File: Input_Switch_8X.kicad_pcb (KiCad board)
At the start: 2 copper layers, 133 x 50 mm, 86 parts, among them J1 Conn_01x02, J10 GND, J2 Conn_01x02, J3 Conn_01x02, J4 Conn_01x02, J5 Conn_01x02, J6 Conn_01x02, J7 Conn_01x02, J8 Conn_01x02, J9 VCC, Q1 AO3400A, Q10 AO3400A, Q11 BC817, Q12 AO3400A, Q13 BC817, Q14 AO3400A, Q15 BC817, Q16 AO3400A, Q2 BC817, Q3 BC817, Q4 AO3400A, Q5 BC817, Q6 AO3400A, Q7 BC817, Q8 AO3400A, Q9 BC817, SW1 SW_Push, SW10 SW_SPST, SW11 SW_Push, SW12 SW_SPST, SW13 SW_Push, SW14 SW_SPST, SW15 SW_Push, SW16 SW_SPST, SW2 SW_SPST, SW3 SW_Push, SW4 SW_SPST, SW5 SW_Push, SW6 SW_SPST, SW7 SW_Push, SW8 SW_SPST, SW9 SW_Push

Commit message: update footprint
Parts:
- D1, D10, D12, D14, D16, D4, D6, D8: footprint LED_SMD:LED_0603_1608Metric -> Library:LED_0603_1608Metric
- H1, H2, H3, H4: footprint MountingHole:MountingHole_3.2mm_M3_Pad_Via -> Library:MountingHole_3.2mm_M3_Pad_Via
- J1, J2, J3, J4, J5, J6, J7, J8: footprint Connector_PinHeader_2.54mm:PinHeader_1x02_P2.54mm_Vertical -> Library:PinHeader_1x02_P2.54mm_Vertical
- J10, J9: footprint Connector_PinHeader_2.54mm:PinHeader_2x02_P2.54mm_Vertical -> Library:PinHeader_2x02_P2.54mm_Vertical
- Q1, Q10, Q11, Q12, Q13, Q14, Q15, Q16, Q2, Q3, Q4, Q5, Q6, Q7, Q8, Q9: footprint Package_TO_SOT_SMD:SOT-23 -> Library:SOT-23
- R1, R10, R11, R12, R13, R14, R15, R16, R17, R18, R19, R2, R20, R21, R22, R23, R24, R3, R4, R5, R6, R7, R8, R9: footprint Resistor_SMD:R_0603_1608Metric -> Library:R_0603_1608Metric
- moved J9 16.4 mm to (78.3, 77.0), turned to 180 degrees
- moved J10 11.5 mm to (78.3, 63.3), turned to 180 degrees
- turned R10 to -90 degrees
- turned R11 to -90 degrees
- turned R12 to -90 degrees
- turned R13 to -90 degrees
- turned R14 to -90 degrees
- turned R16 to -90 degrees
- turned R17 to -90 degrees
- turned R19 to -90 degrees
- turned R20 to -90 degrees
- turned R22 to -90 degrees
- turned R23 to -90 degrees
- turned R8 to -90 degrees
- turned R9 to -90 degrees
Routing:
- net VCC: track 0.00 -> 372.5 mm
- net /Switch_LED_2/Output: track 0.00 -> 54.3 mm, vias 0 -> 1
- net /Switch_LED_5/Output: track 0.00 -> 54.1 mm, vias 0 -> 1
- net /Switch_LED_4/Output: track 0.00 -> 54.1 mm, vias 0 -> 1
- net /Switch_LED_7/Output: track 0.00 -> 54.1 mm, vias 0 -> 1
- net /Switch_LED_6/Output: track 0.00 -> 54.1 mm, vias 0 -> 1
- net /Switch_LED_1/Output: track 0.00 -> 54.1 mm, vias 0 -> 1
- net /Switch_LED_8/Output: track 0.00 -> 54.1 mm, vias 0 -> 1
- net /Switch_LED_3/Output: track 0.00 -> 54.1 mm, vias 0 -> 1
- net Net-(D13-K): track 0.00 -> 12.1 mm
- net Net-(D11-K): track 0.00 -> 12.0 mm
- net Net-(D5-K): track 0.00 -> 12.0 mm
- net Net-(D9-K): track 0.00 -> 11.9 mm
- net Net-(D7-K): track 0.00 -> 11.9 mm
- net Net-(D15-K): track 0.00 -> 11.9 mm
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- added copper zone on B.Cu, net GND
- added copper zone on F.Cu, net GND

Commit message: update
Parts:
- H1, H2, H3, H4: footprint Library:MountingHole_3.2mm_M3_Pad_Via -> MountingHole:MountingHole_3.2mm_M3_Pad_Via
- J10, J9: footprint Library:PinHeader_2x02_P2.54mm_Vertical -> Connector_PinHeader_2.54mm:PinHeader_2x02_P2.54mm_Vertical
- R1, R15, R18, R2, R21, R24, R3, R4: value 33 -> 33R

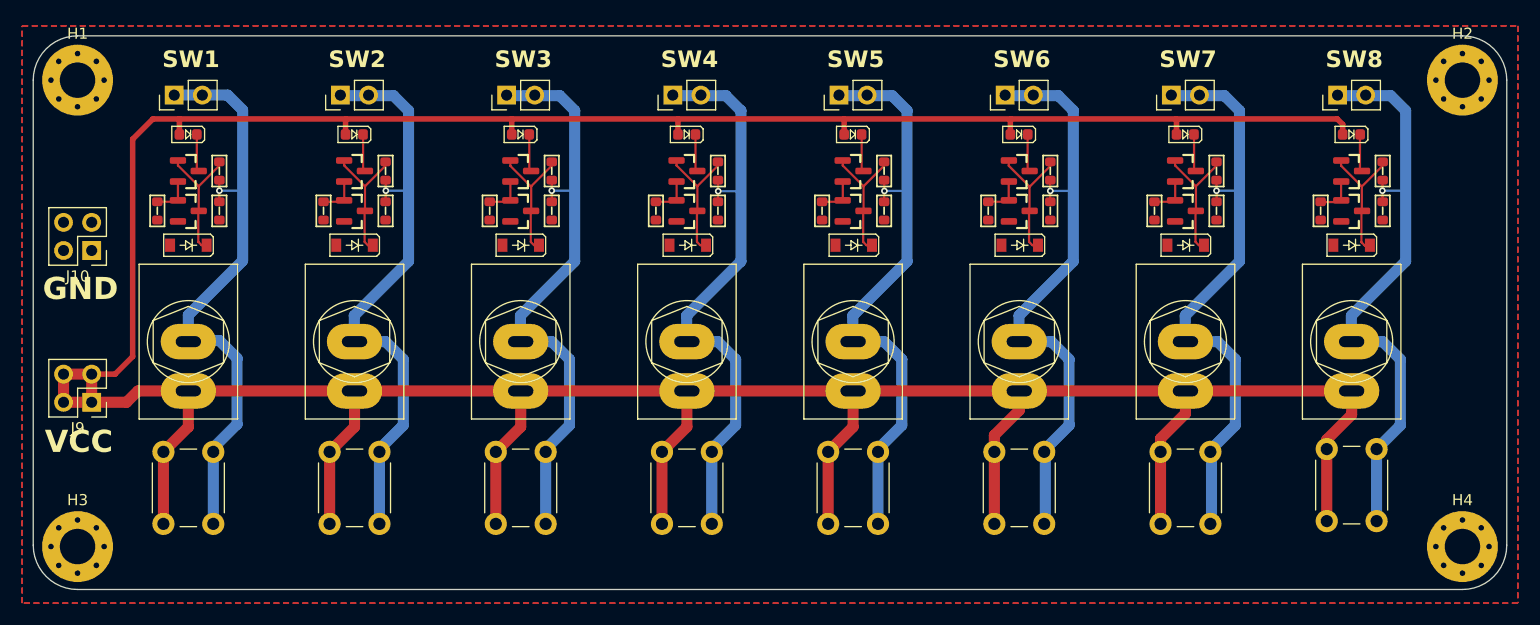
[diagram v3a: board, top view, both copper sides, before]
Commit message: Remove the now ignored directory
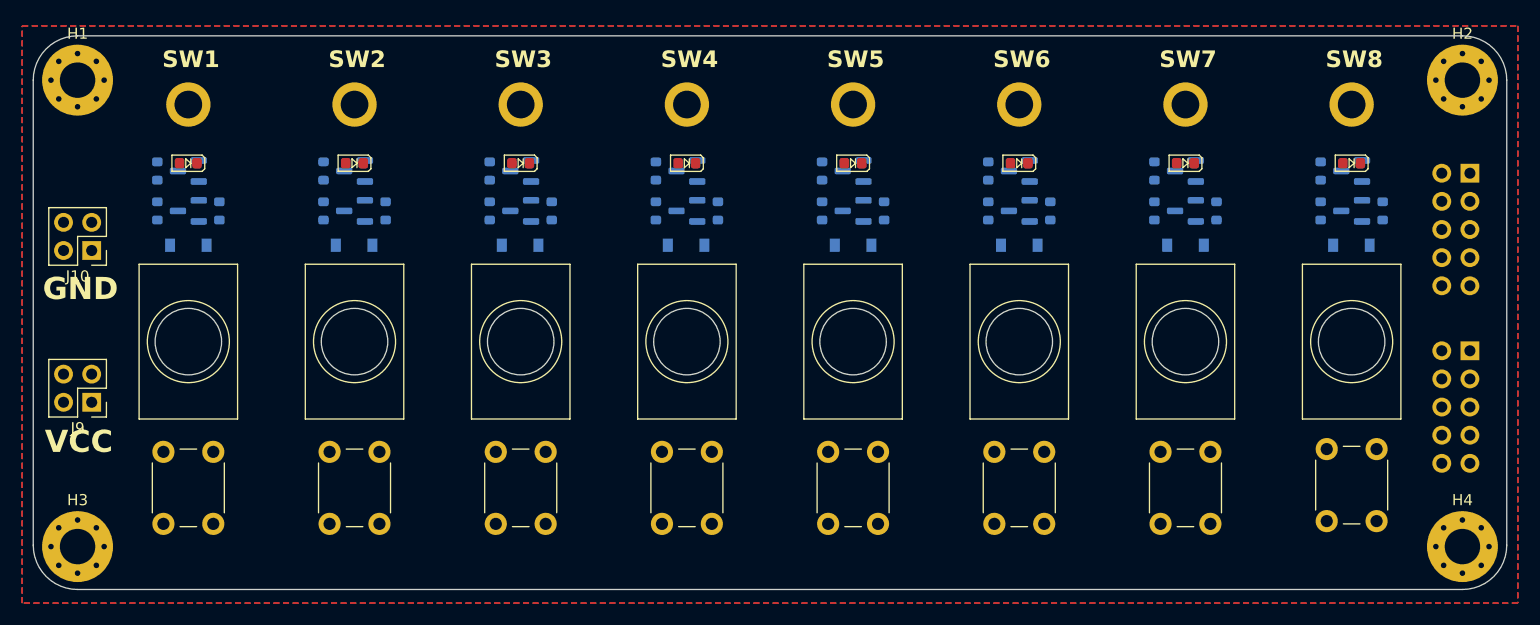
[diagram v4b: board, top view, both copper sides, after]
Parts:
- added REF**: PinHeader_2x05_P2.54mm_Vertical, Library:PinHeader_2x05_P2.54mm_Vertical, B.Cu at (202.7, 72.3)
- added REF**: PinHeader_2x05_P2.54mm_Vertical, Library:PinHeader_2x05_P2.54mm_Vertical, B.Cu at (202.7, 56.3)
- D11, D13, D15, D2, D3, D5, D7, D9, Q1, Q10, Q11, Q12, Q13, Q14, Q15, Q16, Q2, Q3, Q4, Q5, Q6, Q7, Q8, Q9, R1, R10, R11, R12, R13, R14, R15, R16, R17, R18, R19, R2, R20, R21, R22, R23, R24, R3, R4, R5, R6, R7, R8, R9: moved to B.Cu
- H1, H2, H3, H4: footprint MountingHole:MountingHole_3.2mm_M3_Pad_Via -> Library:MountingHole_3.2mm_M3_Pad_Via
- J1, J2, J3, J4, J5, J6, J7, J8: footprint Library:PinHeader_1x02_P2.54mm_Vertical -> Library:MountingHole_2.5mm_Pad
- J10, J9: footprint Connector_PinHeader_2.54mm:PinHeader_2x02_P2.54mm_Vertical -> Library:PinHeader_2x02_P2.54mm_Vertical
- SW10, SW12, SW14, SW16, SW2, SW4, SW6, SW8: footprint Library:SW_Toggle_Blue_wSlots_2_Pins -> Library:SW_Toggle_Blue_wSlots_Nut
- moved R16 65.6 mm to (99.2, 59.7)
- moved R17 65.6 mm to (99.2, 56.1)
- moved R2 65.6 mm to (164.8, 59.7)
- moved D11 60.1 mm to (102.0, 62.8), turned to 0 degrees
- moved D3 60.0 mm to (162.0, 62.8), turned to 0 degrees
- moved Q11 60.0 mm to (102.0, 59.7), turned to 180 degrees
- moved Q12 60.0 mm to (102.0, 56.1), turned to 180 degrees
- moved Q3 60.0 mm to (162.0, 59.7), turned to 180 degrees
- moved Q4 60.0 mm to (162.0, 56.1), turned to 180 degrees
- moved R18 54.4 mm to (104.8, 59.7)
- moved R7 54.4 mm to (159.2, 59.7)
- moved R8 54.4 mm to (159.2, 56.1)
- moved R13 35.6 mm to (114.2, 59.7)
- moved R14 35.6 mm to (114.2, 56.1)
- moved R3 35.6 mm to (149.8, 59.7)
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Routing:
- net VCC: track 372.5 -> 0.00 mm
- net /Switch_LED_2/Output: track 54.3 -> 0.00 mm, vias 1 -> 0
- net /Switch_LED_5/Output: track 54.1 -> 0.00 mm, vias 1 -> 0
- net /Switch_LED_4/Output: track 54.1 -> 0.00 mm, vias 1 -> 0
- net /Switch_LED_7/Output: track 54.1 -> 0.00 mm, vias 1 -> 0
- net /Switch_LED_6/Output: track 54.1 -> 0.00 mm, vias 1 -> 0
- net /Switch_LED_1/Output: track 54.1 -> 0.00 mm, vias 1 -> 0
- net /Switch_LED_8/Output: track 54.1 -> 0.00 mm, vias 1 -> 0
- net /Switch_LED_3/Output: track 54.1 -> 0.00 mm, vias 1 -> 0
- net Net-(D13-K): track 12.1 -> 0.00 mm
- net Net-(D11-K): track 12.0 -> 0.00 mm
- net Net-(D5-K): track 12.0 -> 0.00 mm
- net Net-(D9-K): track 11.9 -> 0.00 mm
- net Net-(D7-K): track 11.9 -> 0.00 mm
- net Net-(D15-K): track 11.9 -> 0.00 mm
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
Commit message: update
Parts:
- added REF**: MountingHole_2.1mm, MountingHole:MountingHole_2.1mm, F.Cu at (77.0, 47.9)
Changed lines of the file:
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@@
 			)
 		)
+		(model "${KIPRJMOD}/3D/24.106.STEP"
+			(offset
+				(xyz 0 0 3.81)
+			)
+			(scale
+				(xyz 1 1 1)
+			)
+			(rotate
+				(xyz 0 0 0)
+			)
+		)
 	)
 	(footprint "Library:MountingHole_2.5mm_Pad"
@@
 			)
 		)
+		(model "${KIPRJMOD}/3D/24.106.STEP"
+			(offset
+				(xyz 0 0 3.81)
+			)
+			(scale
+				(xyz 1 1 1)
+			)
+			(rotate
+				(xyz 0 0 0)
+			)
+		)
 	)
 	(footprint "Library:LED_0603_1608Metric"
@@
 			)
 		)
+		(model "${KIPRJMOD}/3D/24.106.STEP"
+			(offset
+				(xyz 0 0 3.81)
+			)
+			(scale
+				(xyz 1 1 1)
+			)
+			(rotate
+				(xyz 0 0 0)
+			)
+		)
 	)
 	(footprint "Library:SW_Toggle_Blue_wSlots_Nut"
@@
 		)
 	)
+	(footprint "MountingHole:MountingHole_2.1mm"
+		(layer "F.Cu")
+		(at 77 47.9)
+		(descr "Mounting Hole 2.1mm, no annular")
+		(tags "mounting hole 2.1mm no annular")
+		(property "Reference" "REF**"
+			(at 0 -3.2 0)
+			(layer "F.SilkS")
+			(effects
+				(font
+					(size 1 1)
+					(thickness 0.15)
+				)
+			)
+		)
+		(property "Value" "MountingHole_2.1mm"
+			(at 0 3.2 0)
+			(layer "F.Fab")
+			(effects
+				(font
+					(size 1 1)
+					(thickness 0.15)
+				)
+			)
+		)
+		(property "Footprint" "MountingHole:MountingHole_2.1mm"
+			(at 0 0 0)
+			(unlocked yes)
+			(layer "F.Fab")
+			(hide yes)
+			(effects
+				(font
+					(size 1.27 1.27)
+				)
+			)
+		)
+		(property "Datasheet" ""
+			(at 0 0 0)
+			(unlocked yes)
+			(layer "F.Fab")
+			(hide yes)
+			(effects
+				(font
+					(size 1.27 1.27)
+				)
+			)
+		)
+		(property "Description" ""
+			(at 0 0 0)
+			(unlocked yes)
+			(layer "F.Fab")
+			(hide yes)
+			(effects
+				(font
+					(size 1.27 1.27)
+				)
+			)
+		)
+		(attr exclude_from_pos_files exclude_from_bom)
+		(fp_circle
+			(center 0 0)
+			(end 2.1 0)
+			(stroke
+				(width 0.15)
+				(type solid)
+			)
+			(fill none)
+			(layer "Cmts.User")
+		)
+		(fp_circle
+			(center 0 0)
+			(end 2.35 0)
+			(stroke
+				(width 0.05)
+				(type solid)
+			)
+			(fill none)
+			(layer "F.CrtYd")
+		)
+		(fp_text user "${REFERENCE}"
+			(at 0 0 0)
+			(layer "F.Fab")
+			(effects
+				(font
+					(size 1 1)
+					(thickness 0.15)
+				)
+			)
+		)
+		(pad "" np_thru_hole circle
+			(at 0 0)
+			(size 2.1 2.1)
+			(drill 2.1)
+			(layers "*.Cu" "*.Mask")
+		)
+		(model "${KIPRJMOD}/3D/Input_Switch_8X.wrl"
+			(offset
+				(xyz -77 48.5 -12.5)
+			)
+			(scale
+				(xyz 1 1 1)
+			)
+			(rotate
+				(xyz 0 0 0)
+			)
+		)
+	)
 	(footprint "Library:MountingHole_2.5mm_Pad"
 		(layer "F.Cu")
@@
 			)
 		)
+		(model "${KIPRJMOD}/3D/24.106.STEP"
+			(offset
+				(xyz 0 0 3.81)
+			)
+			(scale
+				(xyz 1 1 1)
+			)
+			(rotate
+				(xyz 0 0 0)
+			)
+		)
 	)
 	(footprint "Library:LED_0603_1608Metric"
@@
 			)
 		)
+		(model "${KIPRJMOD}/3D/24.106.STEP"
+			(offset
+				(xyz 0 0 3.81)
+			)
+			(scale
+				(xyz 1 1 1)
+			)
+			(rotate
+				(xyz 0 0 0)
+			)
+		)
 	)
 	(footprint "Library:SW_Toggle_Blue_wSlots_Nut"
@@
 			)
 		)
+		(model "${KIPRJMOD}/3D/24.106.STEP"
+			(offset
+				(xyz 0 0 3.81)
+			)
+			(scale
+				(xyz 1 1 1)
+			)
+			(rotate
+				(xyz 0 0 0)
+			)
+		)
 	)
 	(footprint "Library:SW_Toggle_Blue_wSlots_Nut"
@@
 			)
 		)
+		(model "${KIPRJMOD}/3D/24.106.STEP"
+			(offset
+				(xyz 0 0 3.81)
+			)
+			(scale
+				(xyz 1 1 1)
+			)
+			(rotate
+				(xyz 0 0 0)
+			)
+		)
 	)
 	(footprint "Library:LED_0603_1608Metric"
@@
 			)
 		)
+		(model "${KIPRJMOD}/3D/24.106.STEP"
+			(offset
+				(xyz 0 0 3.81)
+			)
+			(scale
+				(xyz 1 1 1)
+			)
+			(rotate
+				(xyz 0 0 0)
+			)
+		)
